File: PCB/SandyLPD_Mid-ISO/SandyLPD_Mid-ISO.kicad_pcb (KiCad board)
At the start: 2 copper layers, 42.5 x 23.2 mm, 19 parts

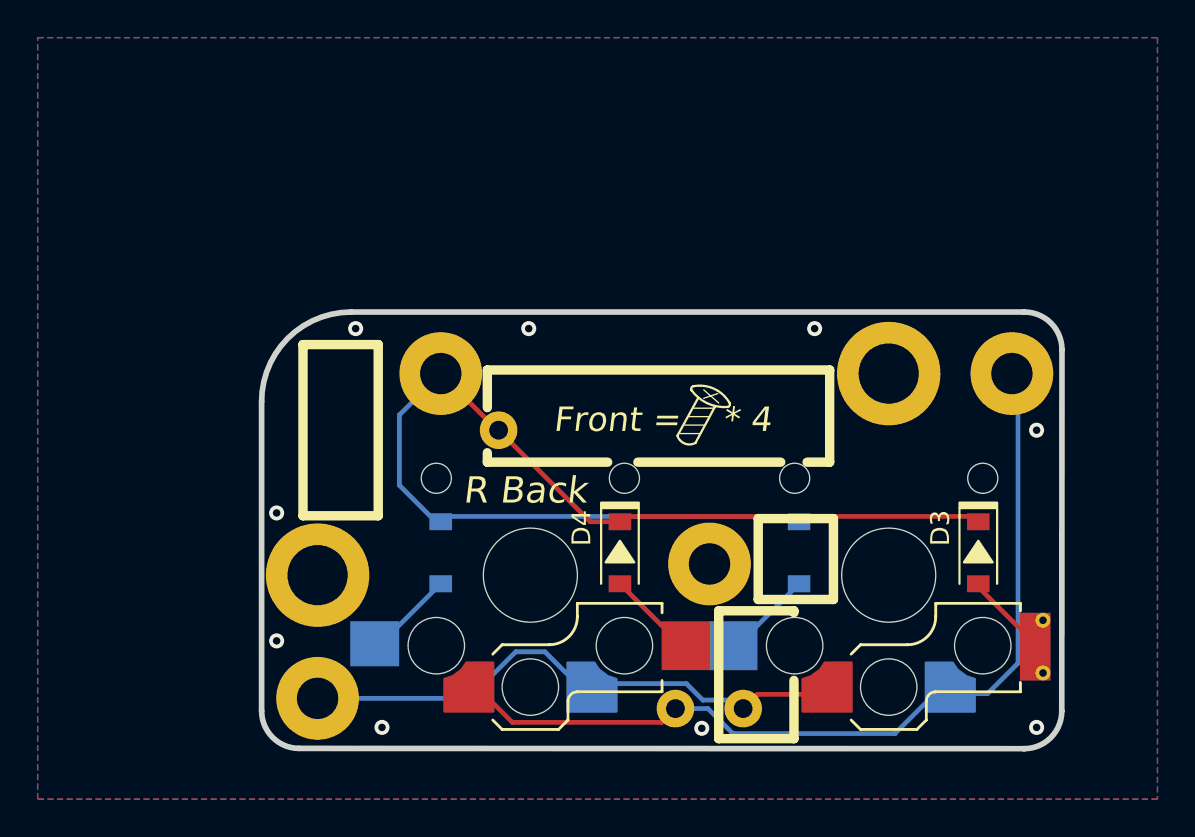
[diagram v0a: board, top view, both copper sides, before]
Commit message: スルーホールタップの接続先を変更・調整 #19
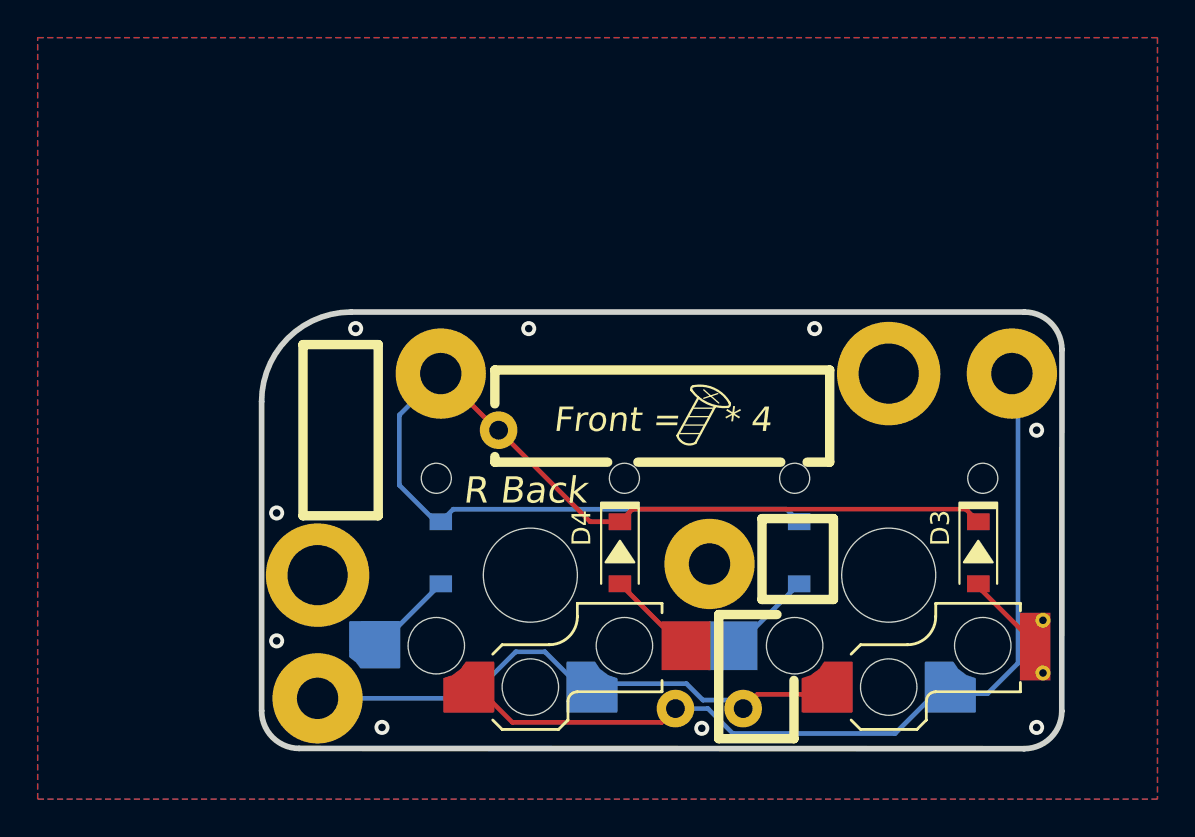
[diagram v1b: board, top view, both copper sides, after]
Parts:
- H1, H2, H3, H4: footprint locallib:MountingHole_2.2mm_M2_Pad_minimal -> locallib:MountingHole_2.2-4.8mm_M2_Pad_minimal_for_Through-hole_tap
- SW_TAB1: footprint locallib:Kailh_socket_ChocV2_for_Reverse_narrow_#2pad -> locallib:Kailh_socket_ChocV2_for_Reverse_narrow_#1_and_#2pad
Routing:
- net LR_Mid-ISO_row0: track 61.2 -> 61.8 mm

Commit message: シルク調整
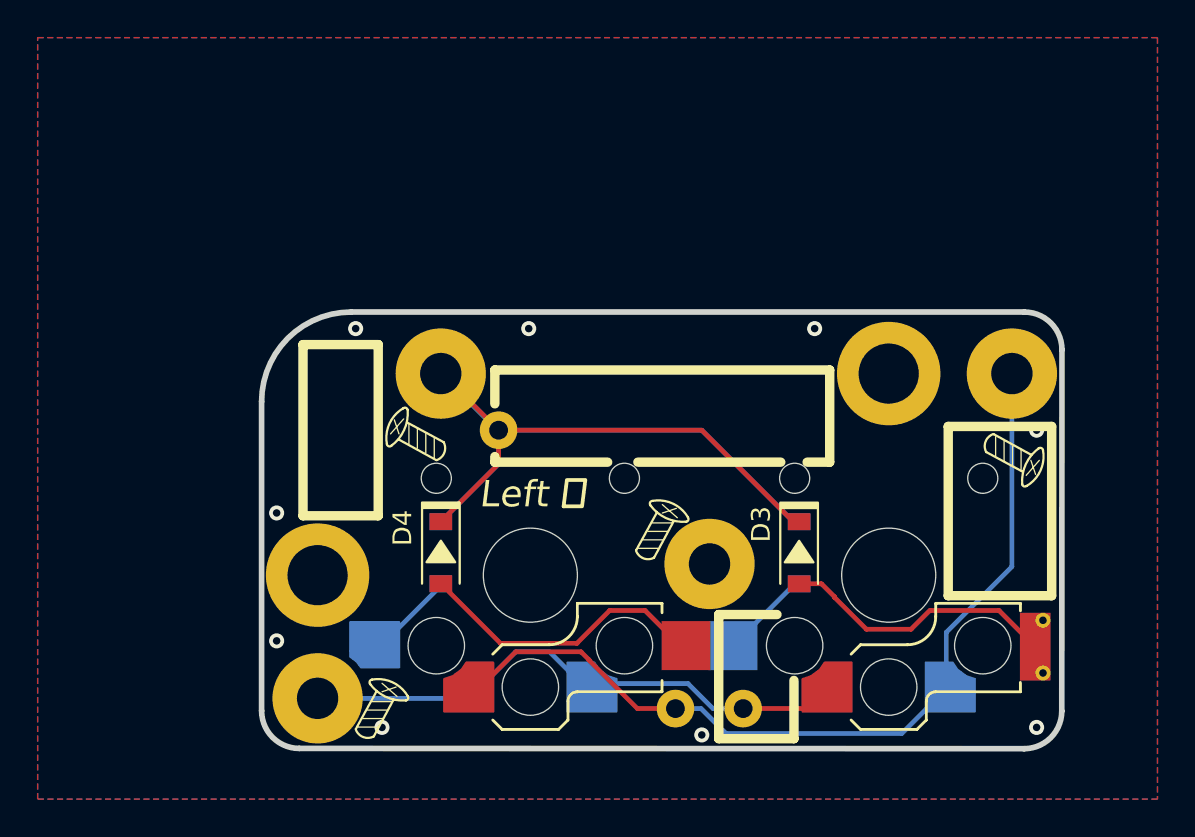
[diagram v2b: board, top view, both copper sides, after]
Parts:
- added REF**: ICON_Screw_Medium, locallib:ICON_Screw_Medium, F.Cu at (32.1, 59.3)
- added REF**: ICON_Screw_Medium, locallib:ICON_Screw_Medium, F.Cu at (63.2, 43.4)
- added REF**: ICON_Screw_Medium, locallib:ICON_Screw_Medium, F.Cu at (47.0, 49.8)
- added REF**: ICON_Screw_Medium, locallib:ICON_Screw_Medium, B.Cu at (32.6, 54.3)
- added REF**: ICON_Screw_Medium, locallib:ICON_Screw_Medium, B.Cu at (46.1, 51.9)
- added REF**: ICON_Screw_Medium, locallib:ICON_Screw_Medium, B.Cu at (69.0, 42.3)
- added REF**: ICON_Screw_Medium, locallib:ICON_Screw_Medium, B.Cu at (32.2, 42.9)
- moved REF** 12.7 mm to (36.6, 42.2), turned to 90 degrees
- moved D3 9.52 mm to (54.4, 48.4)
- moved D4 9.52 mm to (35.4, 48.4)
- turned T_R1 to 0 degrees
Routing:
- net Net-(D4-A): track 4.88 -> 15.8 mm
- net Net-(D3-A): track 4.59 -> 14.8 mm
- net LR_Mid-ISO_row0: track 61.8 -> 56.9 mm
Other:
- board text added: "Left 左"
- board text added: "Right 右"
- board text removed: "Front = * 4"
- board text removed: "L Back"
- board text removed: "R Back"

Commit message: ネジ穴にスルーホールタップのアイコンを追加
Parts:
- added REF**: ICON_Through-hole_Tap, locallib:ICON_Through-hole_Tap, B.Cu at (30.0, 44.3)
- added REF**: ICON_Through-hole_Tap, locallib:ICON_Through-hole_Tap, B.Cu at (59.2, 43.7)
- added REF**: ICON_Through-hole_Tap, locallib:ICON_Through-hole_Tap, F.Cu at (59.2, 43.7)
- added REF**: ICON_Through-hole_Tap, locallib:ICON_Through-hole_Tap, F.Cu at (30.0, 44.3)
- moved REF** 2.45 mm to (45.4, 51.6)
- moved REF** 0.63 mm to (45.6, 51.6)
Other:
- board text added: "Left 左 Back Side"
- board text added: "Right 右 Back Side"
- board text removed: "Left 左"
- board text removed: "Right 右"

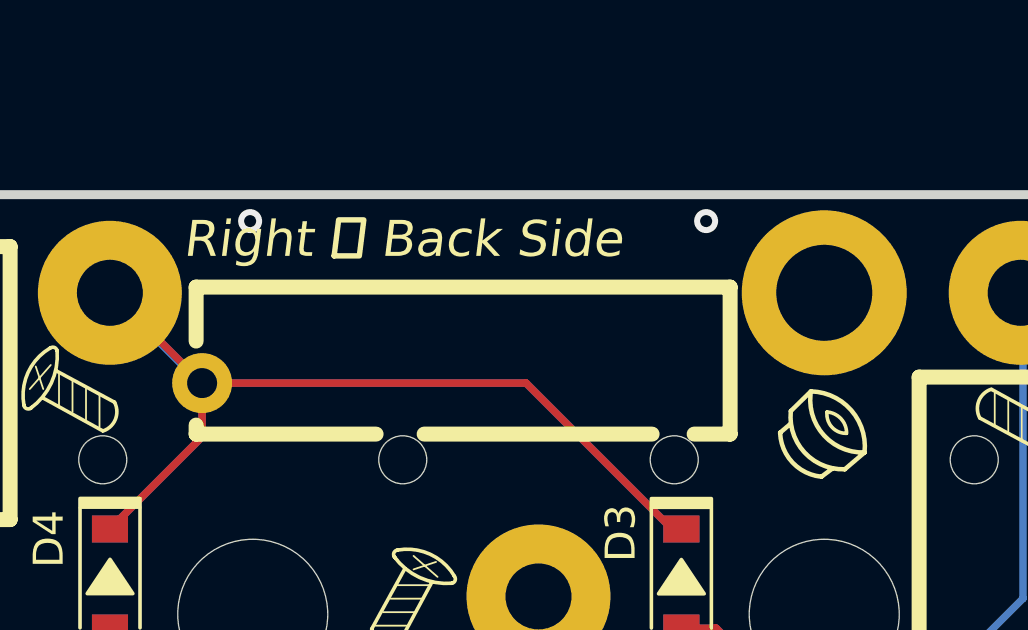
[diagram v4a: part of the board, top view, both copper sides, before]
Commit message: 間違い防止のシルク #30
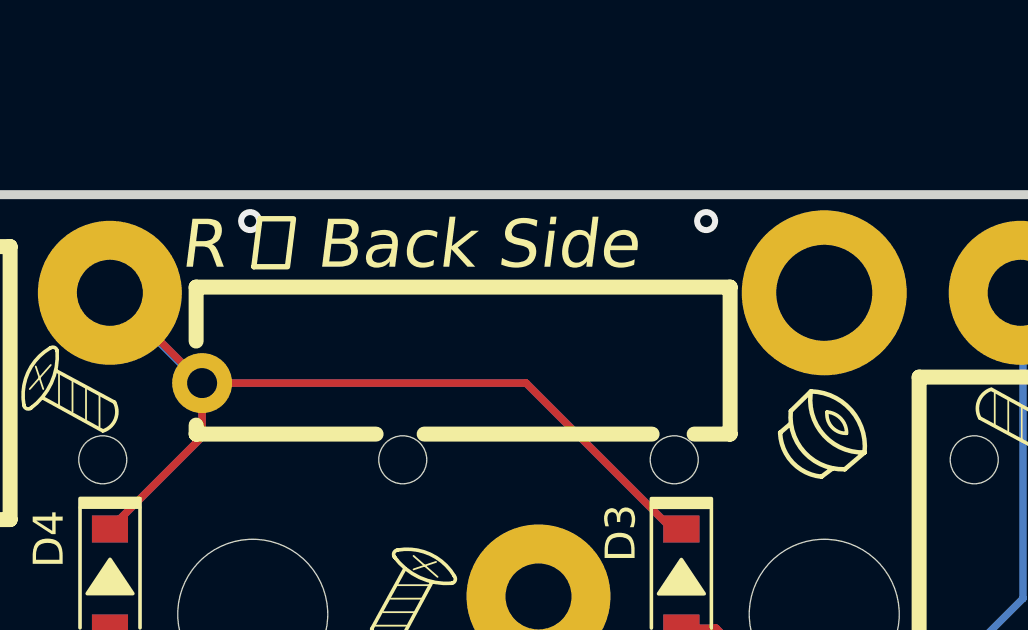
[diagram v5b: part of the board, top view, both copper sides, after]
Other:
- board text added: "L 左 Back Side"
- board text added: "R 右 Back Side"
- board text removed: "Left 左 Back Side"
- board text removed: "Right 右 Back Side"
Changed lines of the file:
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@@
 		(fp_arc
 			(start 0.729448 -0.077979)
-			(mid 0.250509 -0.290344)
+			(mid 0.25051 -0.290344)
 			(end 0.092873 -0.789976)
 			(stroke
@@
 		(fp_arc
 			(start 0.729448 -0.077979)
-			(mid 0.250509 -0.290344)
+			(mid 0.25051 -0.290344)
 			(end 0.092873 -0.789976)
 			(stroke
@@
 			(layer "F.SilkS")
 		)
-		(group ""
-			(members "19ea4f28-b978-4062-834d-26f4fa699d5f" "34327462-1a4f-4c47-a06b-47023dd402e3"
-				"350e3571-9d79-4997-91f3-0c1e3206d9bf" "5f9bc689-d099-4e73-8795-9446c5b2977a"
-				"6f08f226-1e77-4a69-bb49-987aae0fc073" "86608576-f3d8-4a6f-8617-53d05acef3cd"
-				"a75f6955-394c-4a31-b509-dcaa40e77a59" "b305f7d8-95f0-4b72-a0ef-76fcc0196259"
-				"c2a28908-fe6d-4848-a9da-c1a5ceb1845b" "cbad9395-35e8-4017-9c8b-d63ae68e347f"
-			)
-		)
 	)
 	(footprint "locallib:D_SOD-123_Emphasized_Direction_Line"
@@
 			(layer "B.SilkS")
 		)
-		(group ""
-			(members "19ea4f28-b978-4062-834d-26f4fa699d5f" "34327462-1a4f-4c47-a06b-47023dd402e3"
-				"350e3571-9d79-4997-91f3-0c1e3206d9bf" "5f9bc689-d099-4e73-8795-9446c5b2977a"
-				"6f08f226-1e77-4a69-bb49-987aae0fc073" "86608576-f3d8-4a6f-8617-53d05acef3cd"
-				"a75f6955-394c-4a31-b509-dcaa40e77a59" "b305f7d8-95f0-4b72-a0ef-76fcc0196259"
-				"c2a28908-fe6d-4848-a9da-c1a5ceb1845b" "cbad9395-35e8-4017-9c8b-d63ae68e347f"
-			)
-		)
 	)
 	(footprint "locallib:ICON_Screw_Medium"
@@
 			(layer "B.SilkS")
 		)
-		(group ""
-			(members "19ea4f28-b978-4062-834d-26f4fa699d5f" "34327462-1a4f-4c47-a06b-47023dd402e3"
-				"350e3571-9d79-4997-91f3-0c1e3206d9bf" "5f9bc689-d099-4e73-8795-9446c5b2977a"
-				"6f08f226-1e77-4a69-bb49-987aae0fc073" "86608576-f3d8-4a6f-8617-53d05acef3cd"
-				"a75f6955-394c-4a31-b509-dcaa40e77a59" "b305f7d8-95f0-4b72-a0ef-76fcc0196259"
-				"c2a28908-fe6d-4848-a9da-c1a5ceb1845b" "cbad9395-35e8-4017-9c8b-d63ae68e347f"
-			)
-		)
 	)
 	(gr_line
@@
 		(layer "F.SilkS")
 	)
-	(gr_text "Left 左 Back Side"
-		(at 56.583435 37.30028 0)
+	(gr_text "L 左 Back Side"
+		(at 56.383435 37.30028 0)
 		(layer "B.SilkS" knockout)
 		(effects
 			(font
-				(size 1.4 1.4)
+				(size 1.6 1.6)
 				(thickness 0.2)
 				(italic yes)
@@
 		)
 	)
-	(gr_text "Right 右 Back Side"
-		(at 37.783435 37.123715 0)
+	(gr_text "R 右 Back Side"
+		(at 37.683435 37.30028 0)
 		(layer "F.SilkS" knockout)
 		(effects
 			(font
-				(size 1.2 1.2)
+				(size 1.6 1.6)
 				(thickness 0.18)
 				(italic yes)

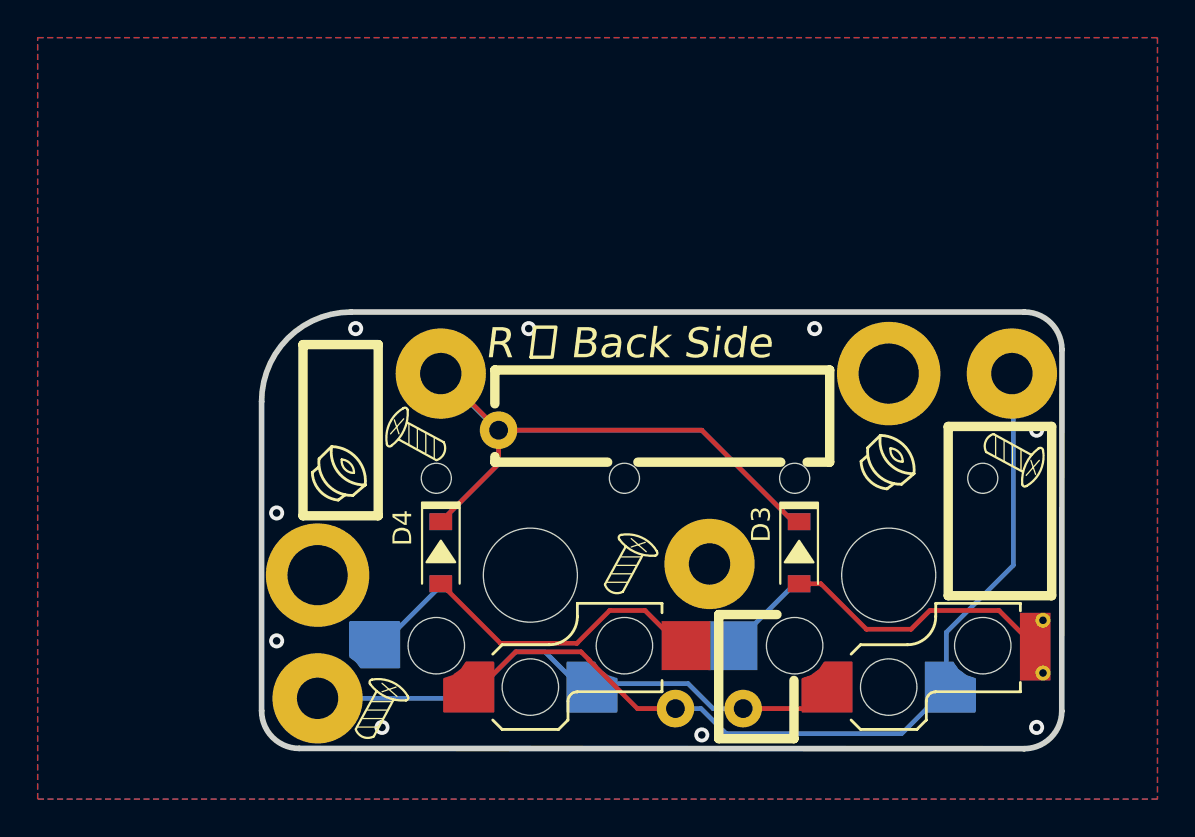
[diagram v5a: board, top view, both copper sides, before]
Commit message: ゴムシート貼り付け指標を調整
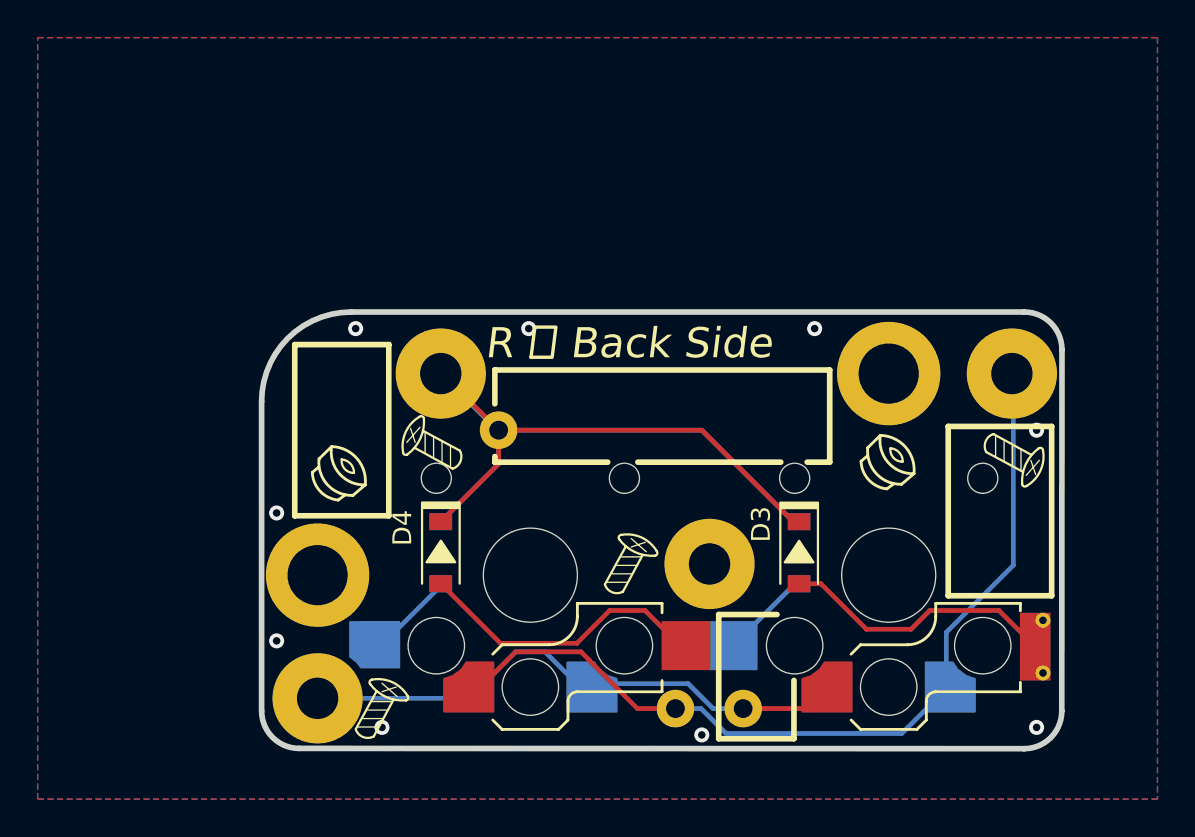
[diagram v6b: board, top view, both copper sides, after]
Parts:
- moved REF** 0.97 mm to (37.5, 42.7)
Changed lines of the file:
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@@
 		(locked yes)
 		(layer "F.Cu")
-		(at 36.600419 42.206339 90)
+		(at 37.462919 42.657589 90)
 		(property "Reference" "REF**"
 			(at 0 0.5 90)
@@
 		(fp_arc
 			(start 0.729448 -0.077979)
-			(mid 0.25051 -0.290344)
+			(mid 0.250512 -0.290345)
 			(end 0.092873 -0.789976)
 			(stroke
@@
 		(fp_arc
 			(start 0.729448 -0.077979)
-			(mid 0.25051 -0.290344)
+			(mid 0.250512 -0.290345)
 			(end 0.092873 -0.789976)
 			(stroke
@@
 		(tags "SOD-123")
 		(property "Reference" "D1"
-			(at -1.315625 2.125 90)
+			(at -0.595306 2.125 90)
 			(layer "B.SilkS")
 			(effects
@@
 		(end 38.220935 38.71903)
 		(stroke
-			(width 0.5)
+			(width 0.3)
 			(type default)
 		)
@@
 		(end 44.220935 43.61903)
 		(stroke
-			(width 0.5)
+			(width 0.3)
 			(type default)
 		)
@@
 		(end 38.220935 38.71903)
 		(stroke
-			(width 0.5)
+			(width 0.3)
 			(type default)
 		)
@@
 	)
 	(gr_rect
-		(start 28.020935 37.36903)
-		(end 32.020935 46.46903)
+		(start 27.583435 37.35028)
+		(end 32.583435 46.45028)
 		(stroke
-			(width 0.5)
+			(width 0.3)
 			(type default)
 		)
@@
 		(end 67.820935 44.41903)
 		(stroke
-			(width 0.5)
+			(width 0.3)
 			(type default)
 		)
@@
 		(end 67.820935 51.51903)
 		(stroke
-			(width 0.5)
+			(width 0.3)
 			(type default)
 		)
@@
 		(end 38.220935 43.61903)
 		(stroke
-			(width 0.5)
+			(width 0.3)
 			(type default)
 		)
@@
 		(end 45.150935 55.21903)
 		(stroke
-			(width 0.5)
+			(width 0.3)
 			(type default)
 		)
@@
 		(end 49.150935 58.31903)
 		(stroke
-			(width 0.5)
+			(width 0.3)
 			(type default)
 		)
@@
 	)
 	(gr_line
-		(start 67.920935 51.36903)
-		(end 67.920935 52.66903)
+		(start 67.873435 51.36028)
+		(end 67.873435 52.66028)
 		(stroke
-			(width 0.3)
+			(width 0.2)
 			(type default)
 		)
@@
 		(end 62.320935 44.41903)
 		(stroke
-			(width 0.5)
+			(width 0.3)
 			(type default)
 		)
@@
 		(end 53.420935 43.61903)
 		(stroke
-			(width 0.5)
+			(width 0.3)
 			(type default)
 		)
@@
 		(end 56.020935 43.61903)
 		(stroke
-			(width 0.5)
+			(width 0.3)
 			(type default)
 		)
@@
 		(end 45.820935 51.71903)
 		(stroke
-			(width 0.5)
+			(width 0.3)
 			(type default)
 		)
@@
 		(end 65.920935 53.81903)
 		(stroke
-			(width 0.5)
+			(width 0.3)
 			(type default)
 		)
@@
 		(end 56.020935 38.71903)
 		(stroke
-			(width 0.5)
+			(width 0.3)
 			(type default)
 		)
@@
 		(end 63.070935 44.41903)
 		(stroke
-			(width 0.5)
+			(width 0.3)
 			(type default)
 		)
@@
 		(end 49.150935 51.71903)
 		(stroke
-			(width 0.5)
+			(width 0.3)
 			(type default)
 		)
@@
 		(end 62.320935 53.81903)
 		(stroke
-			(width 0.5)
+			(width 0.3)
 			(type default)
 		)
@@
 		(end 67.820935 53.81903)
 		(stroke
-			(width 0.5)
+			(width 0.3)
 			(type default)
 		)
@@
 		(end 38.220935 38.71903)
 		(stroke
-			(width 0.5)
+			(width 0.3)
 			(type default)
 		)
@@
 		(end 56.020935 43.61903)
 		(stroke
-			(width 0.5)
+			(width 0.3)
 			(type default)
 		)
@@
 		(end 53.220935 51.71903)
 		(stroke
-			(width 0.5)
+			(width 0.3)
 			(type default)
 		)
@@
 		(end 53.420935 43.61903)
 		(stroke
-			(width 0.5)
+			(width 0.3)
 			(type default)
 		)
@@
 		(end 44.220935 43.61903)
 		(stroke
-			(width 0.5)
+			(width 0.3)
 			(type default)
 		)
@@
 	)
 	(gr_rect
-		(start 28.020935 37.36903)
-		(end 32.020935 46.46903)
+		(start 27.583435 37.36903)
+		(end 32.583435 46.46903)
 		(stroke
-			(width 0.5)
+			(width 0.3)
 			(type default)
 		)
@@
 		(end 54.120935 55.21903)
 		(stroke
-			(width 0.5)
+			(width 0.3)
 			(type default)
 		)
@@
 		(end 50.120935 51.71903)
 		(stroke
-			(width 0.5)
+			(width 0.3)
 			(type default)
 		)
@@
 		(end 56.020935 38.71903)
 		(stroke
-			(width 0.5)
+			(width 0.3)
 			(type default)
 		)
@@
 		(end 38.220935 38.71903)
 		(stroke
-			(width 0.5)
+			(width 0.3)
 			(type default)
 		)
@@
 		(end 38.220935 43.61903)
 		(stroke
-			(width 0.5)
+			(width 0.3)
 			(type default)
 		)
@@
 		(end 50.120935 58.31903)
 		(stroke
-			(width 0.5)
+			(width 0.3)
 			(type default)
 		)
@@
 		(end 67.820935 50.71903)
 		(stroke
-			(width 0.5)
+			(width 0.3)
 			(type default)
 		)
